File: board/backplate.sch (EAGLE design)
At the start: 22 parts, among them IC1 MAX7219CNG, IC2 MAX7219CNG, IC3 MAX7219CNG, IC4 MAX7219CNG

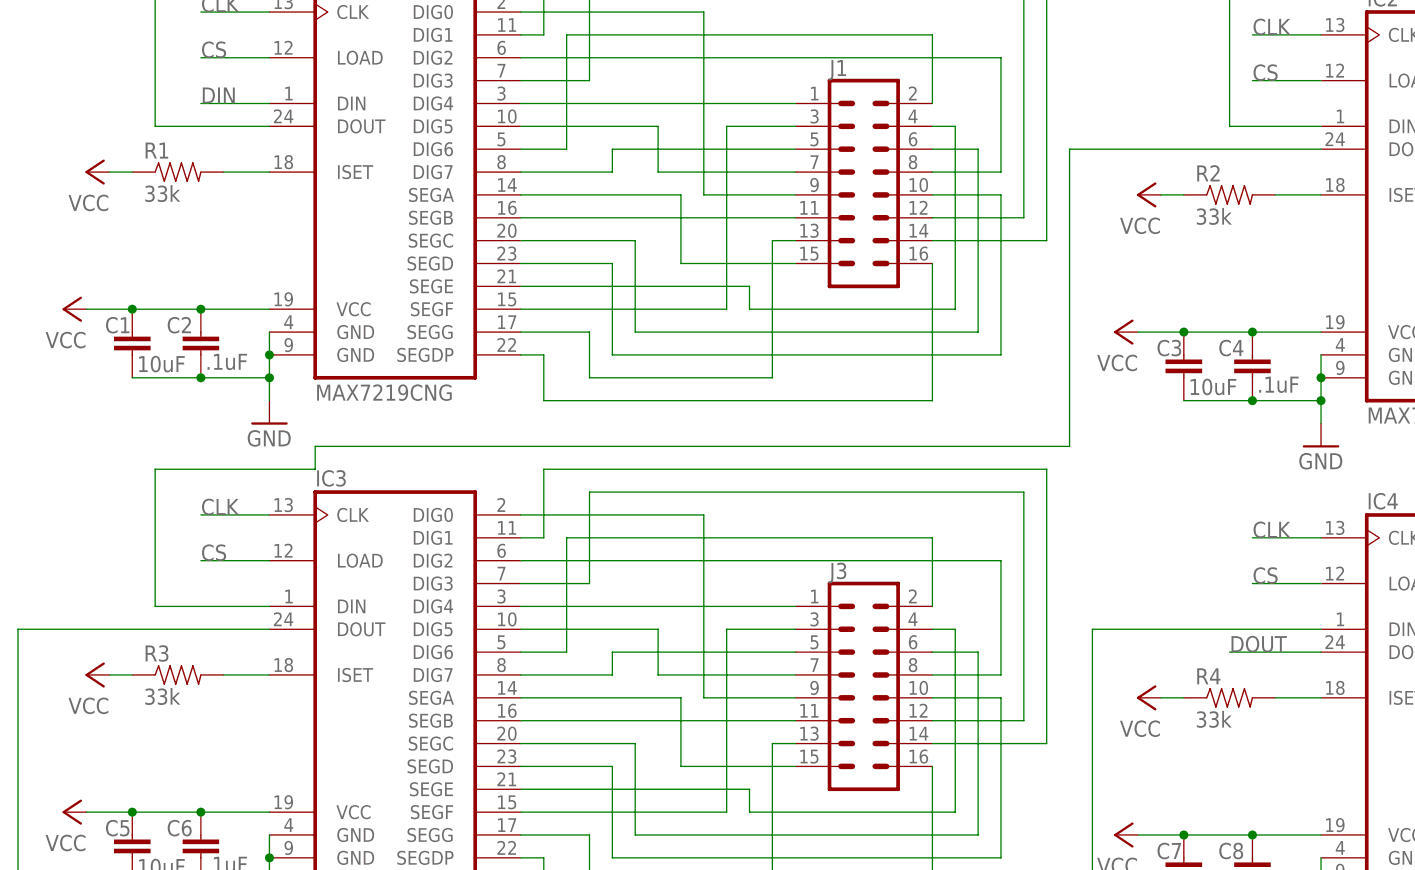
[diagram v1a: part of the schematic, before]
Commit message: changed resistors to thru
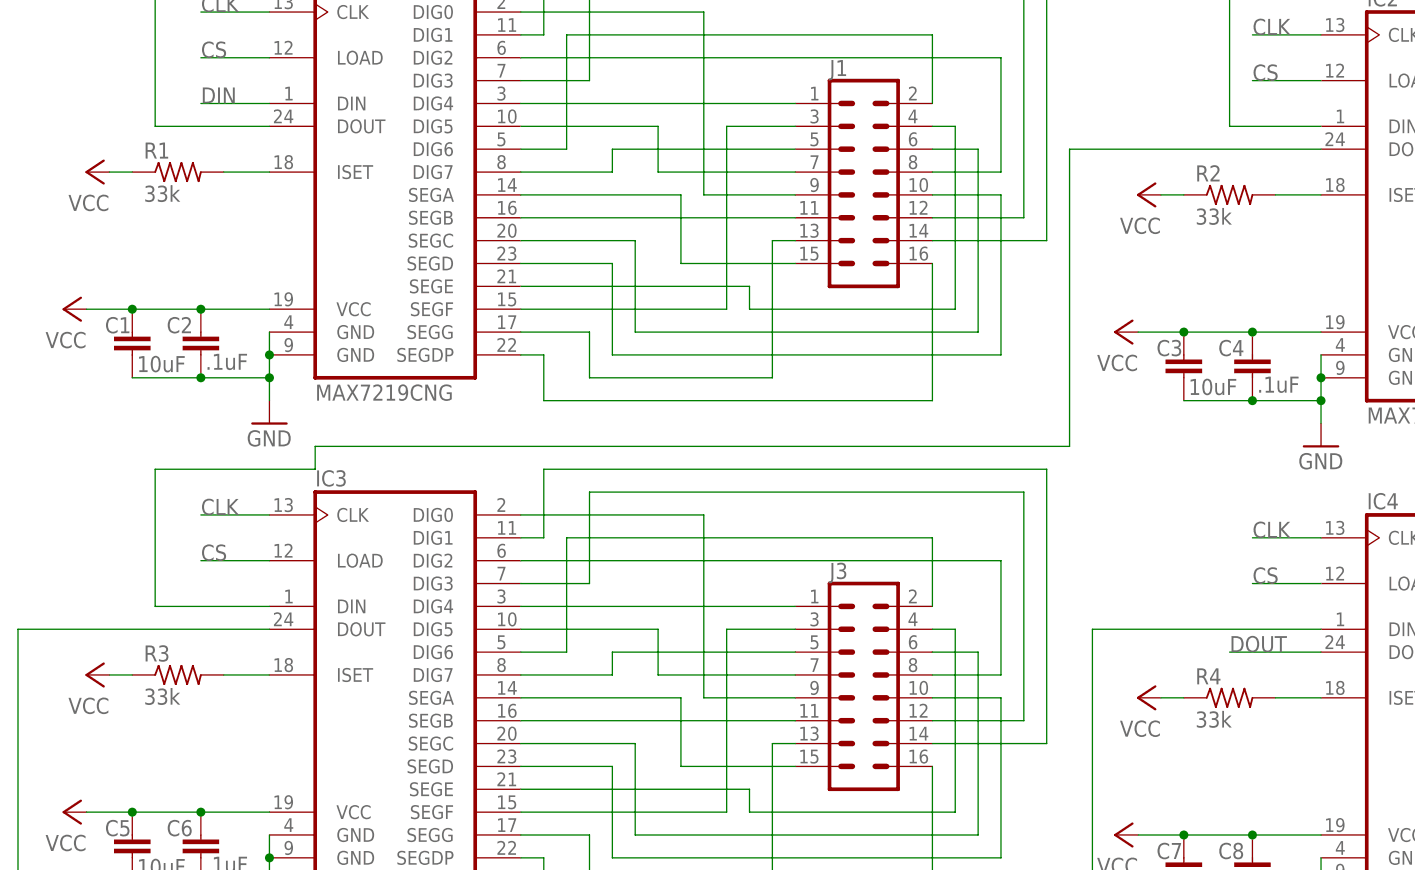
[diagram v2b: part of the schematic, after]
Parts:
- R1, R2, R3, R4: device TinyTony_ShenzenReady:RESISTOR0805-RES -> rcl:R-US_V526-0
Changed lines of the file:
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@@
 <grid distance="0.1" unitdist="inch" unit="inch" style="lines" multiple="1" display="no" altdistance="0.01" altunitdist="inch" altunit="inch"/>
 <layers>
-<layer number="1" name="Top" color="4" fill="1" visible="no" active="no"/>
-<layer number="16" name="Bottom" color="1" fill="1" visible="no" active="no"/>
-<layer number="17" name="Pads" color="2" fill="1" visible="no" active="no"/>
-<layer number="18" name="Vias" color="2" fill="1" visible="no" active="no"/>
-<layer number="19" name="Unrouted" color="6" fill="1" visible="no" active="no"/>
-<layer number="20" name="Dimension" color="15" fill="1" visible="no" active="no"/>
-<layer number="21" name="tPlace" color="7" fill="1" visible="no" active="no"/>
-<layer number="22" name="bPlace" color="7" fill="1" visible="no" active="no"/>
-<layer number="23" name="tOrigins" color="15" fill="1" visible="no" active="no"/>
-<layer number="24" name="bOrigins" color="15" fill="1" visible="no" active="no"/>
-<layer number="25" name="tNames" color="7" fill="1" visible="no" active="no"/>
-<layer number="26" name="bNames" color="7" fill="1" visible="no" active="no"/>
-<layer number="27" name="tValues" color="7" fill="1" visible="no" active="no"/>
-<layer number="28" name="bValues" color="7" fill="1" visible="no" active="no"/>
+<layer number="1" name="Top" color="4" fill="1" visible="yes" active="no"/>
+<layer number="16" name="Bottom" color="1" fill="1" visible="yes" active="no"/>
+<layer number="17" name="Pads" color="2" fill="1" visible="yes" active="no"/>
+<layer number="18" name="Vias" color="2" fill="1" visible="yes" active="no"/>
+<layer number="19" name="Unrouted" color="6" fill="1" visible="yes" active="no"/>
+<layer number="20" name="Dimension" color="24" fill="1" visible="yes" active="no"/>
+<layer number="21" name="tPlace" color="7" fill="1" visible="yes" active="no"/>
+<layer number="22" name="bPlace" color="7" fill="1" visible="yes" active="no"/>
+<layer number="23" name="tOrigins" color="15" fill="1" visible="yes" active="no"/>
+<layer number="24" name="bOrigins" color="15" fill="1" visible="yes" active="no"/>
+<layer number="25" name="tNames" color="7" fill="1" visible="yes" active="no"/>
+<layer number="26" name="bNames" color="7" fill="1" visible="yes" active="no"/>
+<layer number="27" name="tValues" color="7" fill="1" visible="yes" active="no"/>
+<layer number="28" name="bValues" color="7" fill="1" visible="yes" active="no"/>
 <layer number="29" name="tStop" color="7" fill="3" visible="no" active="no"/>
 <layer number="30" name="bStop" color="7" fill="6" visible="no" active="no"/>
@@
 <layer number="35" name="tGlue" color="7" fill="4" visible="no" active="no"/>
 <layer number="36" name="bGlue" color="7" fill="5" visible="no" active="no"/>
-<layer number="37" name="tTest" color="7" fill="1" visible="no" active="no"/>
-<layer number="38" name="bTest" color="7" fill="1" visible="no" active="no"/>
+<layer number="37" name="tTest" color="7" fill="1" visible="yes" active="no"/>
+<layer number="38" name="bTest" color="7" fill="1" visible="yes" active="no"/>
 <layer number="39" name="tKeepout" color="4" fill="11" visible="no" active="no"/>
 <layer number="40" name="bKeepout" color="1" fill="11" visible="no" active="no"/>
@@
 <layer number="44" name="Drills" color="7" fill="1" visible="no" active="no"/>
 <layer number="45" name="Holes" color="7" fill="1" visible="no" active="no"/>
-<layer number="46" name="Milling" color="3" fill="1" visible="no" active="no"/>
-<layer number="47" name="Measures" color="7" fill="1" visible="no" active="no"/>
-<layer number="48" name="Document" color="7" fill="1" visible="no" active="no"/>
-<layer number="49" name="Reference" color="7" fill="1" visible="no" active="no"/>
-<layer number="50" name="dxf" color="7" fill="1" visible="no" active="no"/>
-<layer number="51" name="tDocu" color="7" fill="1" visible="no" active="no"/>
-<layer number="52" name="bDocu" color="7" fill="1" visible="no" active="no"/>
-<layer number="53" name="tGND_GNDA" color="7" fill="1" visible="no" active="no"/>
-<layer number="54" name="bGND_GNDA" color="7" fill="1" visible="no" active="no"/>
-<layer number="56" name="wert" color="7" fill="1" visible="no" active="no"/>
-<layer number="57" name="tCAD" color="7" fill="1" visible="no" active="no"/>
-<layer number="59" name="tCarbon" color="7" fill="1" visible="no" active="no"/>
-<layer number="60" name="bCarbon" color="7" fill="1" visible="no" active="no"/>
+<layer number="46" name="Milling" color="3" fill="1" visible="yes" active="no"/>
+<layer number="47" name="Measures" color="7" fill="1" visible="yes" active="no"/>
+<layer number="48" name="Document" color="7" fill="1" visible="yes" active="no"/>
+<layer number="49" name="Reference" color="7" fill="1" visible="yes" active="no"/>
+<layer number="50" name="dxf" color="7" fill="1" visible="yes" active="no"/>
+<layer number="51" name="tDocu" color="7" fill="1" visible="yes" active="no"/>
+<layer number="52" name="bDocu" color="7" fill="1" visible="yes" active="no"/>
+<layer number="53" name="tGND_GNDA" color="7" fill="1" visible="yes" active="no"/>
+<layer number="54" name="bGND_GNDA" color="7" fill="1" visible="yes" active="no"/>
+<layer number="56" name="wert" color="7" fill="1" visible="yes" active="no"/>
+<layer number="57" name="tCAD" color="7" fill="1" visible="yes" active="no"/>
+<layer number="59" name="tCarbon" color="7" fill="1" visible="yes" active="no"/>
+<layer number="60" name="bCarbon" color="7" fill="1" visible="yes" active="no"/>
 <layer number="88" name="SimResults" color="9" fill="1" visible="yes" active="yes"/>
 <layer number="89" name="SimProbes" color="9" fill="1" visible="yes" active="yes"/>
@@
 <part name="IC1" library="maxim" library_urn="urn:adsk.eagle:library:269" deviceset="MAX7219CNG" device="" package3d_urn="urn:adsk.eagle:package:17515/1"/>
 <part name="FRAME1" library="frames" library_urn="urn:adsk.eagle:library:229" deviceset="A4L-LOC" device=""/>
-<part name="R1" library="TinyTony_ShenzenReady" library_urn="urn:adsk.eagle:library:2159173" deviceset="RESISTOR" device="0805-RES" package3d_urn="urn:adsk.eagle:package:2160663/2" value="33k"/>
+<part name="R1" library="rcl" library_urn="urn:adsk.eagle:library:334" deviceset="R-US_" device="V526-0" package3d_urn="urn:adsk.eagle:package:23590/1" value="33k"/>
 <part name="P+1" library="supply1" library_urn="urn:adsk.eagle:library:371" deviceset="VCC" device=""/>
 <part name="P+2" library="supply1" library_urn="urn:adsk.eagle:library:371" deviceset="VCC" device=""/>
@@
 <part name="J1" library="SparkFun-Connectors" library_urn="urn:adsk.eagle:library:513" deviceset="CONN_08X2" device="" package3d_urn="urn:adsk.eagle:package:38152/1"/>
 <part name="IC2" library="maxim" library_urn="urn:adsk.eagle:library:269" deviceset="MAX7219CNG" device="" package3d_urn="urn:adsk.eagle:package:17515/1"/>
-<part name="R2" library="TinyTony_ShenzenReady" library_urn="urn:adsk.eagle:library:2159173" deviceset="RESISTOR" device="0805-RES" package3d_urn="urn:adsk.eagle:package:2160663/2" value="33k"/>
+<part name="R2" library="rcl" library_urn="urn:adsk.eagle:library:334" deviceset="R-US_" device="V526-0" package3d_urn="urn:adsk.eagle:package:23590/1" value="33k"/>
 <part name="P+3" library="supply1" library_urn="urn:adsk.eagle:library:371" deviceset="VCC" device=""/>
 <part name="P+4" library="supply1" library_urn="urn:adsk.eagle:library:371" deviceset="VCC" device=""/>
@@
 <part name="J2" library="SparkFun-Connectors" library_urn="urn:adsk.eagle:library:513" deviceset="CONN_08X2" device="" package3d_urn="urn:adsk.eagle:package:38152/1"/>
 <part name="IC3" library="maxim" library_urn="urn:adsk.eagle:library:269" deviceset="MAX7219CNG" device="" package3d_urn="urn:adsk.eagle:package:17515/1"/>
-<part name="R3" library="TinyTony_ShenzenReady" library_urn="urn:adsk.eagle:library:2159173" deviceset="RESISTOR" device="0805-RES" package3d_urn="urn:adsk.eagle:package:2160663/2" value="33k"/>
+<part name="R3" library="rcl" library_urn="urn:adsk.eagle:library:334" deviceset="R-US_" device="V526-0" package3d_urn="urn:adsk.eagle:package:23590/1" value="33k"/>
 <part name="P+5" library="supply1" library_urn="urn:adsk.eagle:library:371" deviceset="VCC" device=""/>
 <part name="P+6" library="supply1" library_urn="urn:adsk.eagle:library:371" deviceset="VCC" device=""/>
@@
 <part name="J3" library="SparkFun-Connectors" library_urn="urn:adsk.eagle:library:513" deviceset="CONN_08X2" device="" package3d_urn="urn:adsk.eagle:package:38152/1"/>
 <part name="IC4" library="maxim" library_urn="urn:adsk.eagle:library:269" deviceset="MAX7219CNG" device="" package3d_urn="urn:adsk.eagle:package:17515/1"/>
-<part name="R4" library="TinyTony_ShenzenReady" library_urn="urn:adsk.eagle:library:2159173" deviceset="RESISTOR" device="0805-RES" package3d_urn="urn:adsk.eagle:package:2160663/2" value="33k"/>
+<part name="R4" library="rcl" library_urn="urn:adsk.eagle:library:334" deviceset="R-US_" device="V526-0" package3d_urn="urn:adsk.eagle:package:23590/1" value="33k"/>
 <part name="P+7" library="supply1" library_urn="urn:adsk.eagle:library:371" deviceset="VCC" device=""/>
 <part name="P+8" library="supply1" library_urn="urn:adsk.eagle:library:371" deviceset="VCC" device=""/>
@@
 packages will not be understood (or retained) with this version.
 </note>
+<note version="8.4" severity="warning">
+Since Version 8.4, EAGLE supports properties for SPICE simulation.
+Probes in schematics and SPICE mapping objects found in parts and library devices
+will not be understood with this version. Update EAGLE to the latest version
+for full support of SPICE simulation.
+</note>
 </compatibility>

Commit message: backplight v2
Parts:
- JP1, JP2: device pinhead:PINHD-1X55X2MM -> SparkFun-Connectors:CONN_05
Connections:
- removed net N$13 (its old number): IC1.DIG3, J1.12
- removed net N$17: IC1.SEGA, J1.15
- removed net N$19 (its old number): IC2.DIG4, J2.1
- removed net N$20 (its old number): IC2.DIG6, J2.2
- removed net N$29: IC2.DIG3, J2.12
- removed net N$31: IC2.DIG1, J2.14
- removed net N$33 (its old number): IC2.SEGA, J2.15
- removed net N$34: IC2.DIG2, J2.8
- removed net N$40 (its old number): IC3.DIG7, J3.5
- removed net N$41 (its old number): IC3.SEGC, J3.6
- removed net N$58 (its old number): IC4.SEGC, J4.6
- removed net N$59 (its old number): IC4.DIG5, J4.7
- removed net N$63: IC4.DIG3, J4.12
- removed net N$65: IC4.DIG1, J4.14
- removed net N$68: IC4.DIG2, J4.8
- new net N$2: IC1.SEGD, J1.13
- new net N$28: IC2.DIG6, J2.4
- new net N$35: IC2.SEGD, J2.13
- new net N$45: IC3.DIG2, J3.16
- new net N$62: IC4.DIG1, J4.5
- new net N$69: IC4.DIG5, J4.14
- new net N$71: IC1.SEGC, J1.12
- new net N$72: IC4.DIG6, J4.4
- new net N$73: IC4.DIG7, J4.10
- new net N$74: IC4.SEGA, J4.3
- new net N$76: IC4.SEGD, J4.13
- new net N$77: IC4.SEGE, J4.8
- new net N$78: IC4.SEGF, J4.6
- new net N$79: IC4.SEGG, J4.7
- new net N$80: IC4.SEGDP, J4.1
- net N$10: now also IC1.DIG7; no longer IC1.SEGD
- net N$11: now also IC1.SEGA, J1.3; no longer IC1.DIG0, J1.9
- net N$14: now also IC1.SEGE, J1.8; no longer IC1.SEGG, J1.13
- net N$15: now also IC1.SEGF, J1.6; no longer IC1.DIG1, J1.14
- net N$16: now also IC1.SEGG, J1.7; no longer IC1.SEGDP, J1.16
- net N$18: now also IC1.SEGDP, J1.1; no longer IC1.DIG2, J1.8
- net N$21: now also IC2.SEGC, J2.12; no longer IC2.SEGF, J2.3
- net N$22: now also IC2.DIG0, J2.15; no longer IC2.SEGE, J2.4
- net N$23: now also IC2.DIG1; no longer IC2.DIG7
- net N$24: now also IC2.DIG2, J2.16; no longer IC2.SEGC, J2.6
- net N$25: now also IC2.DIG3, J2.9; no longer IC2.DIG5, J2.7
- net N$26: now also IC2.DIG4, J2.2; no longer IC2.SEGD, J2.10
- net N$27: now also IC2.DIG5, J2.14; no longer IC2.DIG0, J2.9
- net N$3: now also IC1.DIG0, J1.15; no longer IC1.DIG4, J1.1
- net N$30: now also IC2.DIG7, J2.10; no longer IC2.SEGG, J2.13
- net N$32: now also IC2.SEGA, J2.3; no longer IC2.SEGDP, J2.16
- net N$36: now also IC2.SEGE, J2.8; no longer IC3.DIG4, J3.1
- net N$37: now also IC2.SEGF, J2.6; no longer IC3.DIG6, J3.2
- net N$38: now also IC2.SEGG, J2.7; no longer IC3.SEGF, J3.3
- net N$39: now also IC2.SEGDP, J2.1; no longer IC3.SEGE, J3.4
- net N$4: now also IC1.DIG1, J1.5; no longer IC1.DIG6, J1.2
- net N$42: now also IC3.SEGC, J3.12; no longer IC3.DIG5, J3.7
- net N$43: now also IC3.DIG0, J3.15; no longer IC3.SEGD, J3.10
- net N$44: now also IC3.DIG1, J3.5; no longer IC3.DIG0, J3.9
- net N$46: now also J3.9; no longer J3.12
- net N$47: now also IC3.DIG4, J3.2; no longer IC3.SEGG, J3.13
- net N$48: now also IC3.DIG5; no longer IC3.DIG1
- net N$49: now also IC3.DIG6, J3.4; no longer IC3.SEGDP, J3.16
- net N$5: now also IC1.DIG2, J1.16; no longer IC1.SEGF, J1.3
- net N$50: now also IC3.DIG7, J3.10; no longer IC3.SEGA, J3.15
- net N$51: now also IC3.SEGA, J3.3; no longer IC3.DIG2, J3.8
- net N$53: now also IC3.SEGD, J3.13; no longer IC4.DIG4, J4.1
- net N$54: now also IC3.SEGE, J3.8; no longer IC4.DIG6, J4.2
- net N$55: now also IC3.SEGF, J3.6; no longer IC4.SEGF, J4.3
- net N$56: now also IC3.SEGG, J3.7; no longer IC4.SEGE, J4.4
- net N$57: now also IC3.SEGDP, J3.1; no longer IC4.DIG7, J4.5
- net N$6: now also IC1.DIG3, J1.9; no longer IC1.SEGE, J1.4
- net N$60: now also IC4.SEGC, J4.12; no longer IC4.SEGD, J4.10
- net N$61: now also J4.15; no longer J4.9
- net N$64: now also IC4.DIG2, J4.16; no longer IC4.SEGG, J4.13
- net N$66: now also IC4.DIG3, J4.9; no longer IC4.SEGDP, J4.16
- net N$67: now also IC4.DIG4, J4.2; no longer IC4.SEGA, J4.15
- net N$7: now also IC1.DIG4, J1.2; no longer IC1.DIG7, J1.5
- net N$8: now also IC1.DIG5, J1.14; no longer IC1.SEGC, J1.6
- net N$9: now also IC1.DIG6, J1.4; no longer IC1.DIG5, J1.7
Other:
- note removed: "https://i.imgur.com/5x2sXNw.png pins"
- moved on the sheet: C1, C2, C3, C4, C5, C6, C7, C8, IC1, IC2, IC3, IC4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

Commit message: based on https://i.imgur.com/TE96g29.png" "
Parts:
- removed C3, C5, C7: 10uF, TinyTony_ShenzenReady:CAP0805
- removed C4, C6, C8: .1uF, TinyTony_ShenzenReady:CAP0805
- removed IC2, IC3, IC4: MAX7219CNG, maxim:MAX7219CNG
- removed J2, J3, J4: (no value), SparkFun-Connectors:CONN_08X2
- removed R2, R3, R4: 33k, rcl:R-US_V526-0
- J1: device SparkFun-Connectors:CONN_08X2 -> backplate:CONN_08X2IC
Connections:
- removed net N$18: IC1.SEGDP, J1.1
- removed net N$19: IC2.ISET, R2.2
- removed net N$20: IC2.DOUT, IC3.DIN
- removed net N$21: IC2.SEGC, J2.12
- removed net N$22: IC2.DIG0, J2.15
- removed net N$23: IC2.DIG1, J2.5
- removed net N$24: IC2.DIG2, J2.16
- removed net N$25: IC2.DIG3, J2.9
- removed net N$26: IC2.DIG4, J2.2
- removed net N$27: IC2.DIG5, J2.14
- removed net N$28: IC2.DIG6, J2.4
- removed net N$3 (its old number): IC1.DIG0, J1.15
- removed net N$30: IC2.DIG7, J2.10
- removed net N$32: IC2.SEGA, J2.3
- removed net N$33: IC2.SEGB, J2.11
- removed net N$35: IC2.SEGD, J2.13
- removed net N$36: IC2.SEGE, J2.8
- removed net N$37: IC2.SEGF, J2.6
- removed net N$38: IC2.SEGG, J2.7
- removed net N$39: IC2.SEGDP, J2.1
- removed net N$40: IC3.ISET, R3.2
- removed net N$41: IC1.DOUT, IC2.DIN
- removed net N$42: IC3.SEGC, J3.12
- removed net N$43: IC3.DIG0, J3.15
- removed net N$44: IC3.DIG1, J3.5
- removed net N$45: IC3.DIG2, J3.16
- removed net N$46: IC3.DIG3, J3.9
- removed net N$47: IC3.DIG4, J3.2
- removed net N$48: IC3.DIG5, J3.14
- removed net N$49: IC3.DIG6, J3.4
- removed net N$50: IC3.DIG7, J3.10
- removed net N$51: IC3.SEGA, J3.3
- removed net N$52: IC3.SEGB, J3.11
- removed net N$53: IC3.SEGD, J3.13
- removed net N$54: IC3.SEGE, J3.8
- removed net N$55: IC3.SEGF, J3.6
- removed net N$56: IC3.SEGG, J3.7
- removed net N$57: IC3.SEGDP, J3.1
- removed net N$58: IC4.ISET, R4.2
- removed net N$59: IC3.DOUT, IC4.DIN
- removed net N$60: IC4.SEGC, J4.12
- removed net N$61: IC4.DIG0, J4.15
- removed net N$62: IC4.DIG1, J4.5
- removed net N$64: IC4.DIG2, J4.16
- removed net N$66: IC4.DIG3, J4.9
- removed net N$67: IC4.DIG4, J4.2
- removed net N$69: IC4.DIG5, J4.14
- removed net N$71: IC1.SEGC, J1.12
- removed net N$72: IC4.DIG6, J4.4
- removed net N$73: IC4.DIG7, J4.10
- removed net N$74: IC4.SEGA, J4.3
- removed net N$75: IC4.SEGB, J4.11
- removed net N$76: IC4.SEGD, J4.13
- removed net N$77: IC4.SEGE, J4.8
- removed net N$78: IC4.SEGF, J4.6
- removed net N$79: IC4.SEGG, J4.7
- removed net N$8 (its old number): IC1.DIG5, J1.14
- removed net N$80: IC4.SEGDP, J4.1
- new net N$12: IC1.SEGC, J1.10
- new net N$17: IC1.SEGDP, J1.16
- new net N$4: IC1.DIG2, J1.7
- new net N$9: IC1.DIG7, J1.2
- net CLK: no longer IC2.CLK, IC3.CLK, IC4.CLK
- net CS: no longer IC2.LOAD, IC3.LOAD, IC4.LOAD
- net DOUT: now also IC1.DOUT; no longer IC4.DOUT
- net GND: no longer C3.2, C4.2, C5.2, C6.2, C7.2, C8.2, IC2.GND@1, IC2.GND@2, IC3.GND@1, IC3.GND@2, IC4.GND@1, IC4.GND@2
- net N$10: now also IC1.SEGA, J1.6; no longer IC1.DIG7, J1.10
- net N$11: now also IC1.SEGB, J1.15; no longer IC1.SEGA, J1.3
- net N$13: now also IC1.SEGD, J1.1; no longer IC1.SEGB, J1.11
- net N$14: now also J1.13; no longer J1.8
- net N$15: now also J1.3; no longer J1.6
- net N$16: now also J1.9; no longer J1.7
- net N$2: now also IC1.DIG0, J1.8; no longer IC1.SEGD, J1.13
- net N$5: now also IC1.DIG3, J1.14; no longer IC1.DIG2, J1.16
- net N$6: now also IC1.DIG4, J1.11; no longer IC1.DIG3, J1.9
- net N$7: now also IC1.DIG5, J1.12; no longer IC1.DIG4, J1.2
- net VCC: no longer C3.1, C4.1, C5.1, C6.1, C7.1, C8.1, IC2.VCC, IC3.VCC, IC4.VCC, R2.1, R3.1, R4.1
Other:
- moved on the sheet: J1
